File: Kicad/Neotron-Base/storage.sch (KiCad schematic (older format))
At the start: 8 parts, among them J701 micro SD Card, U401 74LS14

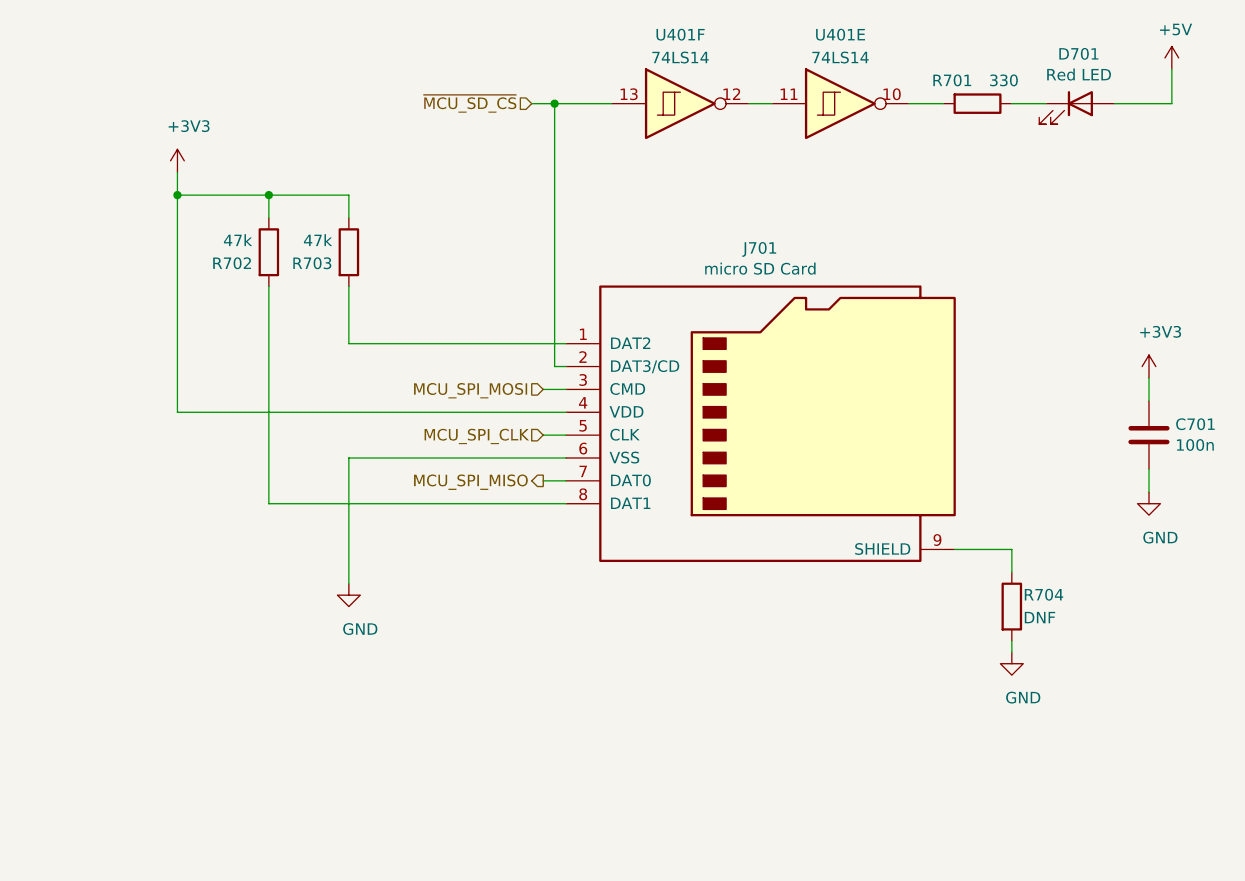
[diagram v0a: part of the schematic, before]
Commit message: Re-work CPU interface to include RMII.
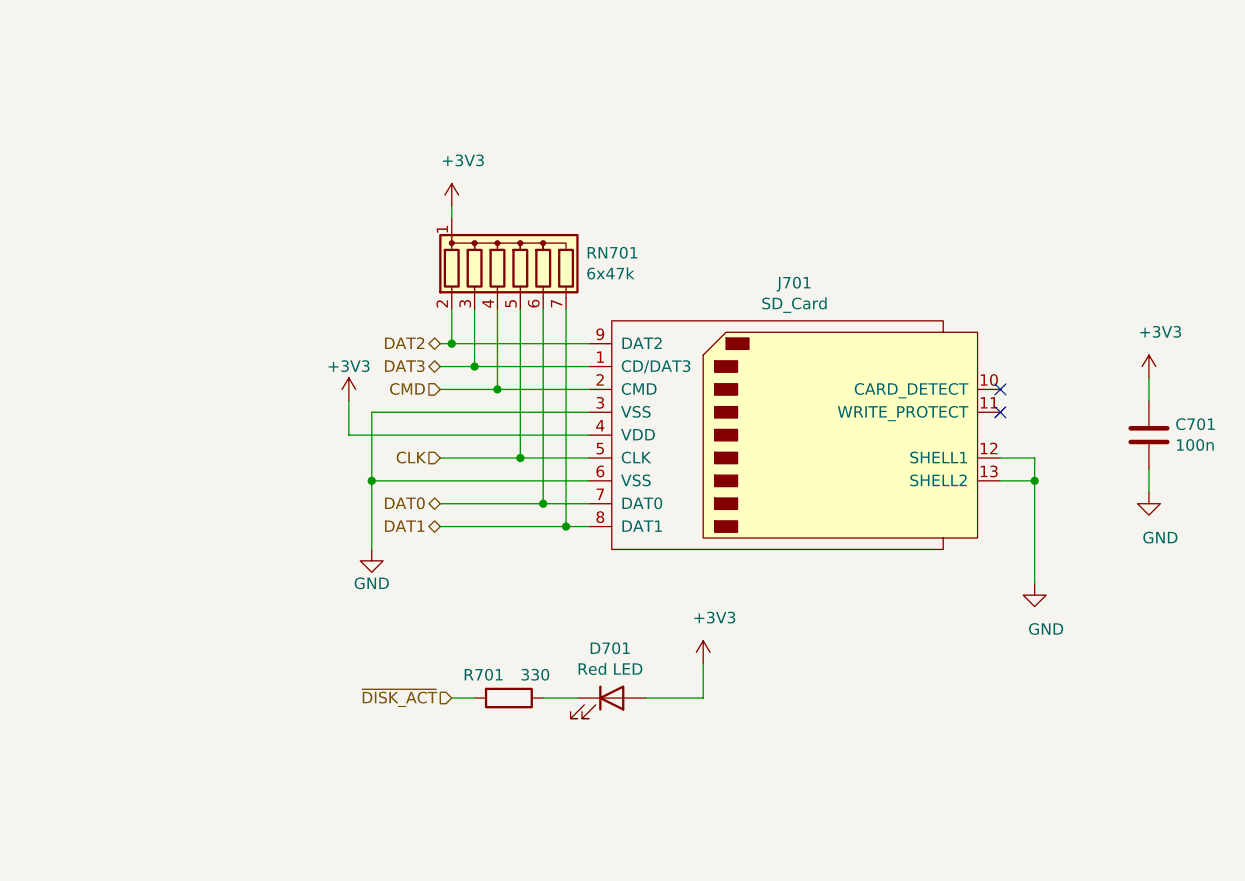
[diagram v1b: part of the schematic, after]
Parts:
- removed J701: micro SD Card, Neotron 32:Molex_4730_2651, symbol Connector:Micro_SD_Card
- removed R702, R703: 47k, Resistor_THT:R_Axial_DIN0207_L6.3mm_D2.5mm_P10.16mm_Horizontal, symbol Device:R
- removed R704: DNF, Resistor_THT:R_Axial_DIN0207_L6.3mm_D2.5mm_P10.16mm_Horizontal, symbol Device:R
- removed U401: 74LS14, Package_DIP:DIP-14_W7.62mm, symbol 74xx:74LS14
- added J701: SD_Card, symbol Connector:SD_Card
- added RN701: 6x47k, Resistor_THT:R_Array_SIP7, symbol Device:R_Network06
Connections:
- net +5V is gone; now on net +3V3: D701.2 (A)
- net +3V3: now also J701.4 (VDD), RN701.1 (common)
- net GND: now also J701.12 (SHELL1), J701.13 (SHELL2), J701.3 (VSS), J701.6 (VSS)
- net ~DISK_ACT: now reaches R701.2
- new net CLK: J701.5 (CLK), RN701.5 (R4)
- new net CMD: J701.2 (CMD), RN701.4 (R3)
- new net DAT0: J701.7 (DAT0), RN701.6 (R5)
- new net DAT1: J701.8 (DAT1), RN701.7 (R6)
- new net DAT2: J701.9 (DAT2), RN701.2 (R1)
- new net DAT3: J701.1 (CD/DAT3), RN701.3 (R2)
- no-connect marks 0 -> 2
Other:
- moved on the sheet: D701, R701
